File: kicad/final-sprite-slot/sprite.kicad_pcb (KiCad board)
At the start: 4 copper layers, 35 x 44.6 mm, 65 parts, among them J1 M20-7910442R, U1 CC430F513X, U2 LSM9DS1, U3 SPRITETCXO_TCXO_7Z, U4 DRV8837, U5 ADP5092, U6 DRV8837, U7 DRV8837, X1 SPRITEPIN_SPRITE_PIN, X2 SPRITEPIN_SPRITE_PIN

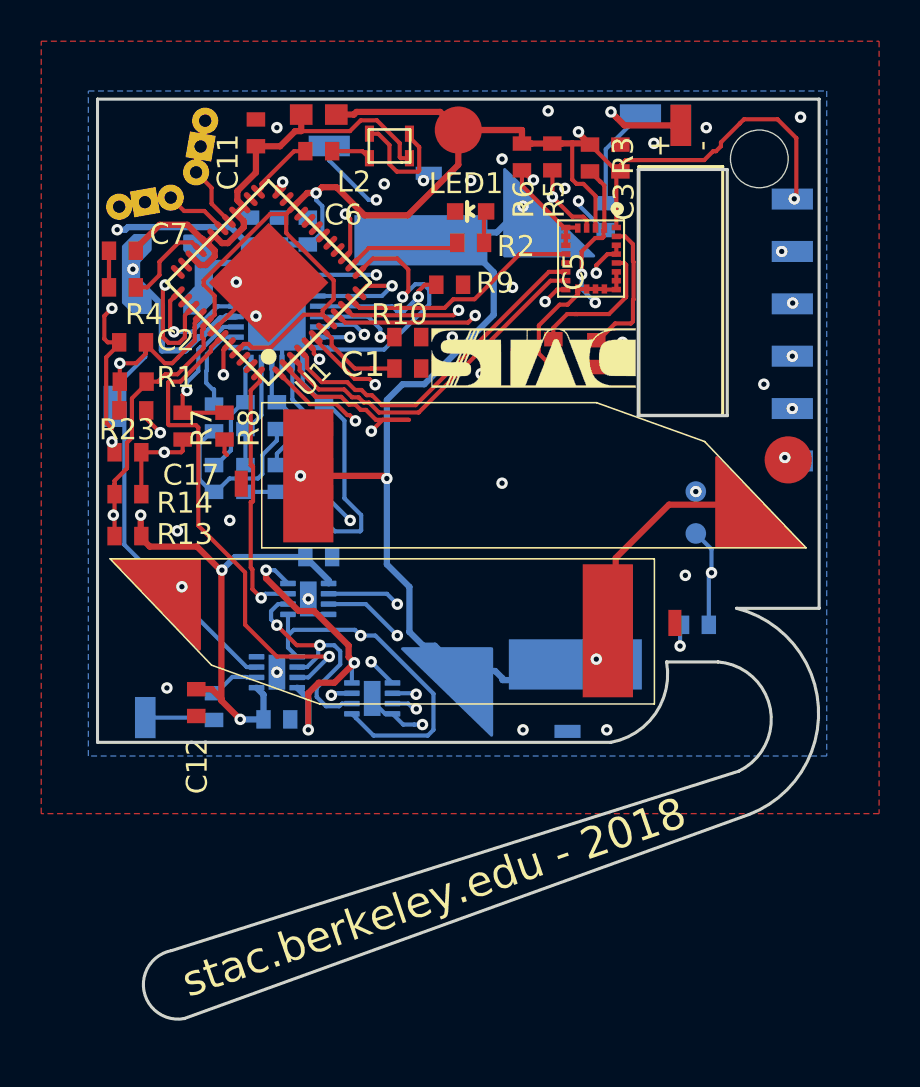
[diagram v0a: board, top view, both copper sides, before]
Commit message: Remove via-in-pad
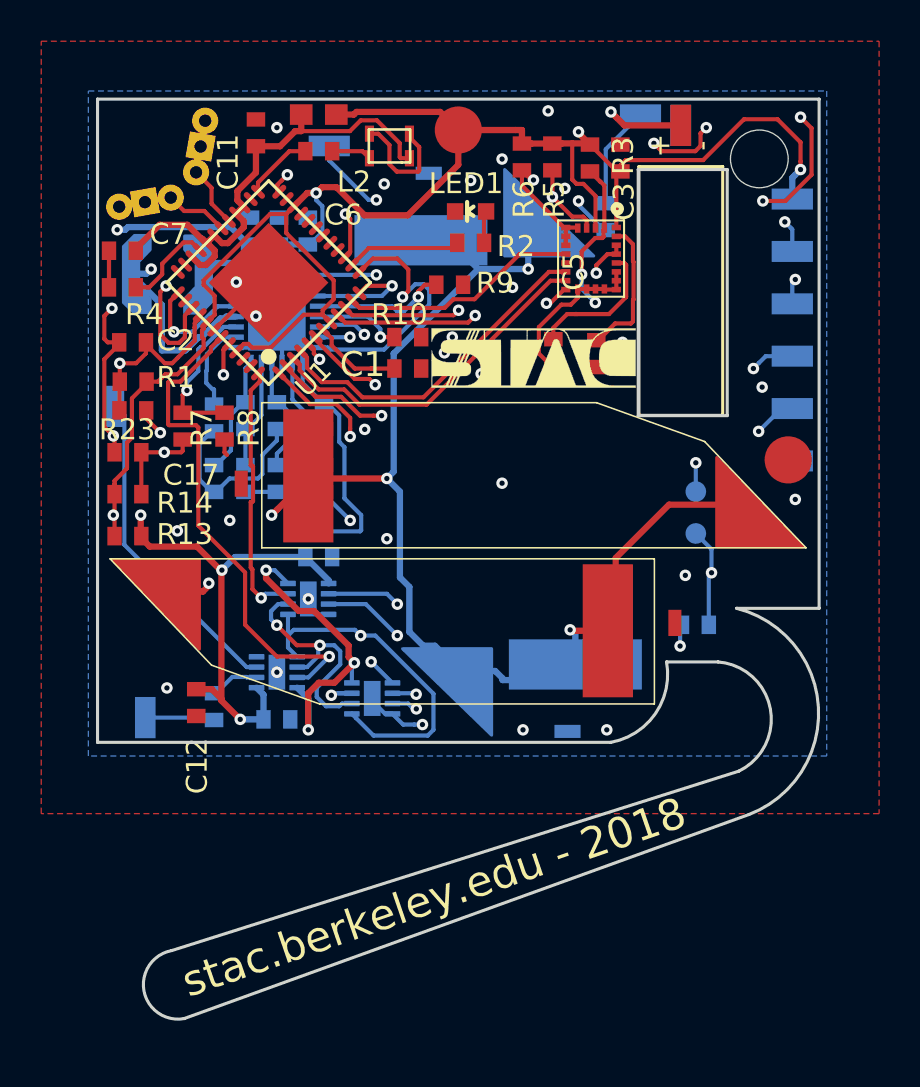
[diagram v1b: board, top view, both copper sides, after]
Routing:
- net GND: track 46.4 -> 57.1 mm, vias 31 -> 34
- net Net-(L3-Pad1): track 19.4 -> 15.9 mm
- net VCCINT: track 96.6 -> 99.4 mm
- net /PWM2: track 36.4 -> 33.8 mm
- net /EN_2: track 21.4 -> 22.2 mm
- net Net-(R22-Pad1): track 432.3 -> 433.2 mm
- net Net-(R12-Pad1): track 32.8 -> 32.0 mm
- net /UART_TX: track 51.7 -> 52.5 mm
